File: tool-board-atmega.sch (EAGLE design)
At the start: 85 parts, among them IC3 ATMEGA2560-16AU, IC4 ATMEGA8U2-MU, Q1 16MHz, Q2 16MHz, X1 22-23-2031, X3 22-23-2031, X4 22-23-2031, X5 22-23-2021, X6 22-23-2021, X7 22-23-2021, X8 22-23-2021, X9 22-23-2101, Y1 16MHz, Y2 16MHz

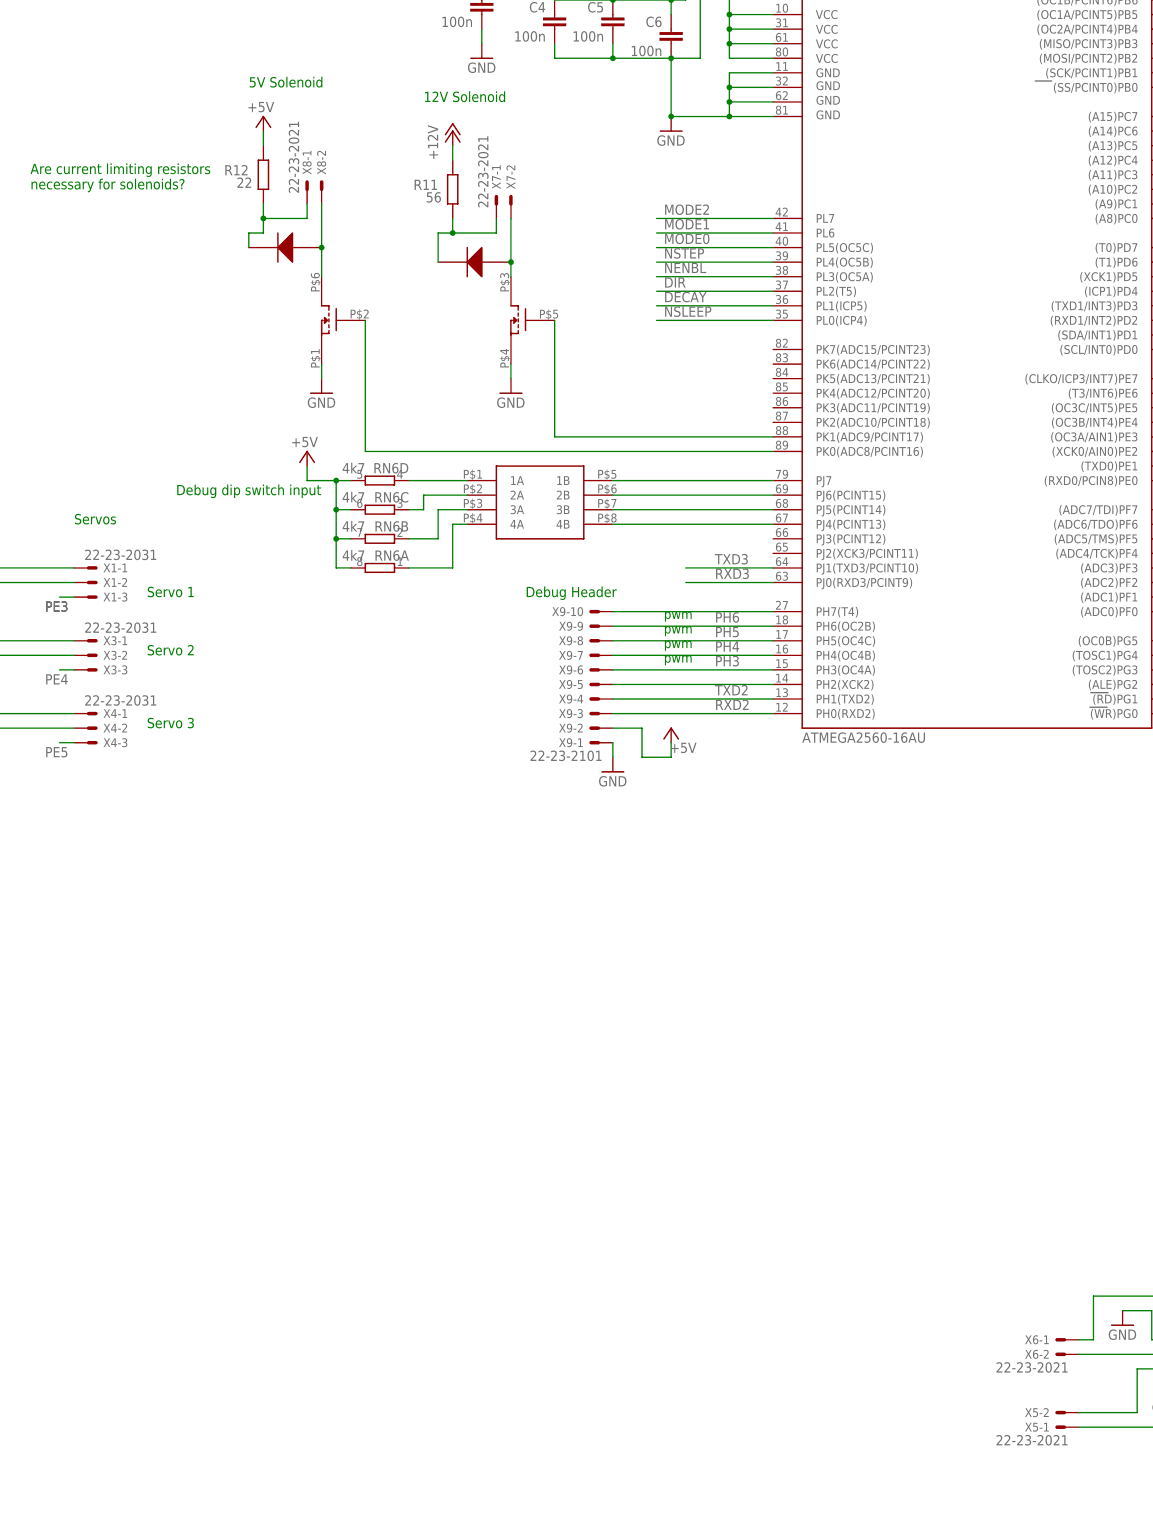
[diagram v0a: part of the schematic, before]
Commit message: board outline planned, some larger parts placed, schematic naming tweaks
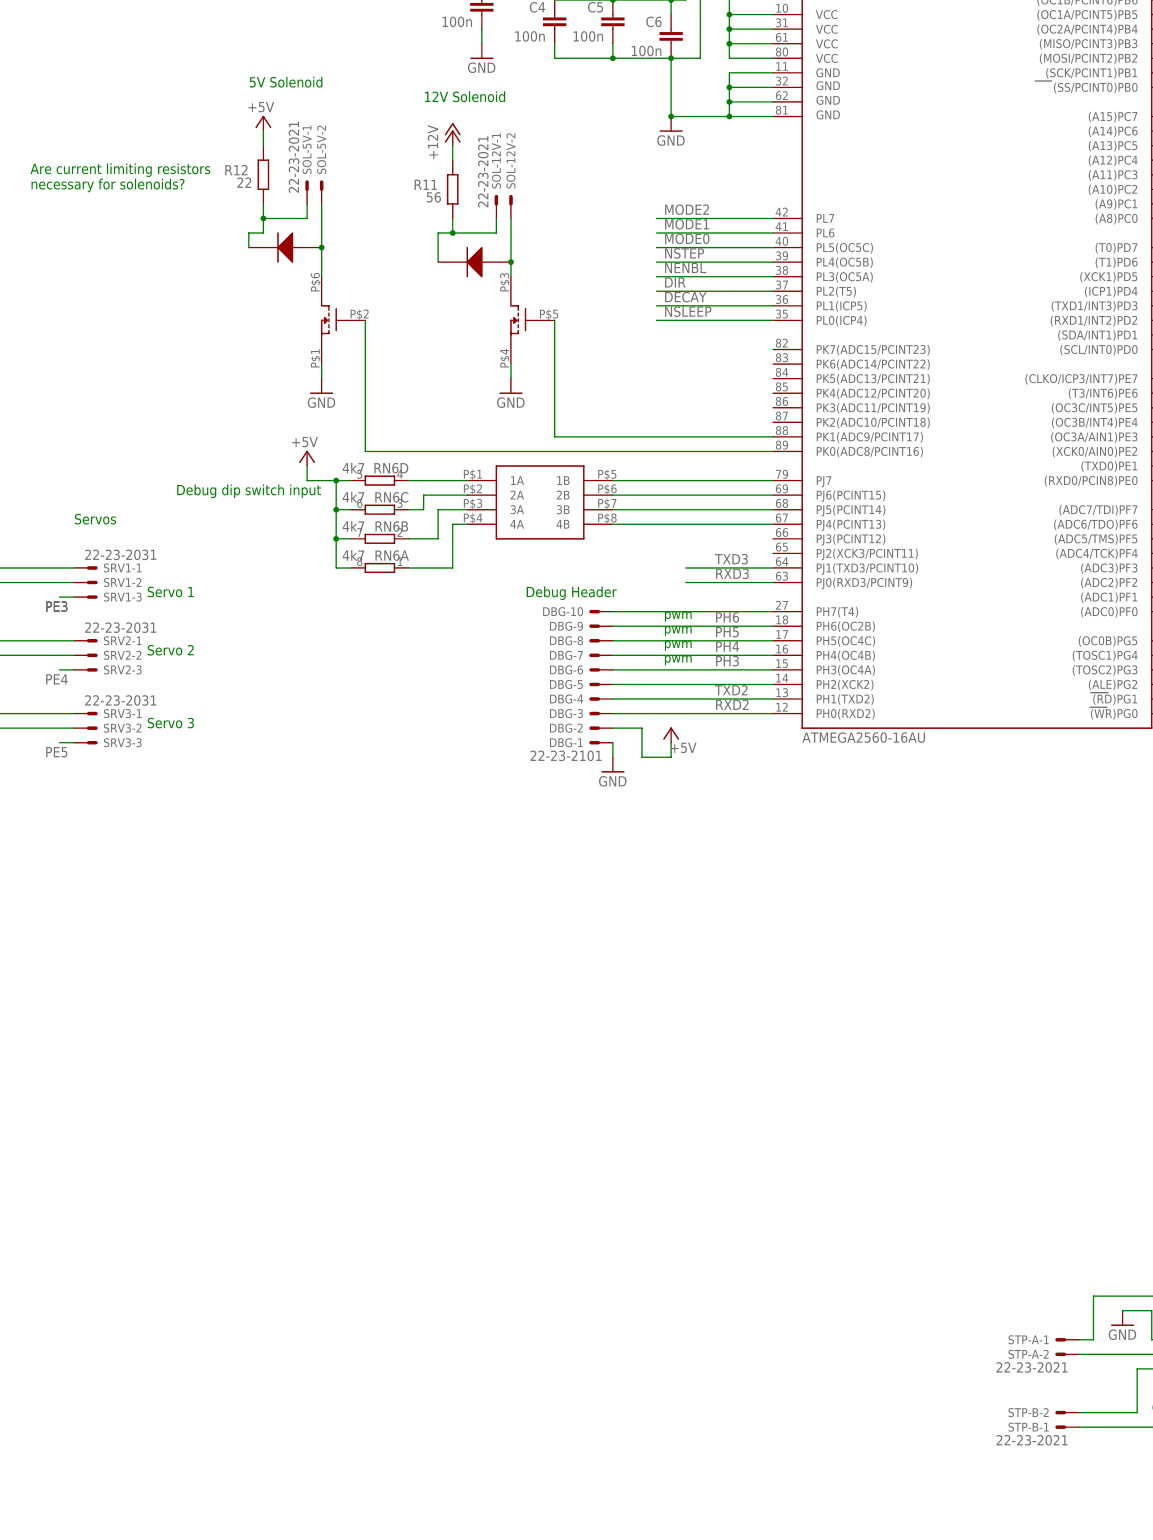
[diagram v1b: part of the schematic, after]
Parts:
- renumbered X1 to SRV1, X3 to SRV2, X4 to SRV3, X5 to STP-B, X6 to STP-A, X7 to SOL-12V, X8 to SOL-5V, X9 to DBG

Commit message: schematic revision edits - thanks Jaden
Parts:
- removed R5: 27R, SmartPrj:R-EU_R0603
- added R13, R15: 1M, SmartPrj:R-EU_R0603
- added R14, R16: 100, SmartPrj:R-EU_R0603
- RN6: value 4k7 -> 2k2
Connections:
- new net N$2: R14.1, U$15G$1.G
- new net N$36: R16.1, U$15G$2.G
- net +5V: no longer RN6A.2, RN6B.2, RN6C.2, RN6D.2
- net GND: now also R13.2, R15.2, RN6A.2, RN6B.2, RN6C.2, RN6D.2
- net N$15: now also R15.1, R16.2; no longer U$15G$2.G
- net N$16: now also R13.1, R14.2; no longer U$15G$1.G
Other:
- moved on the sheet: R11, R12, SOL-12V-1, SOL-12V-2, SOL-5V-1, SOL-5V-2

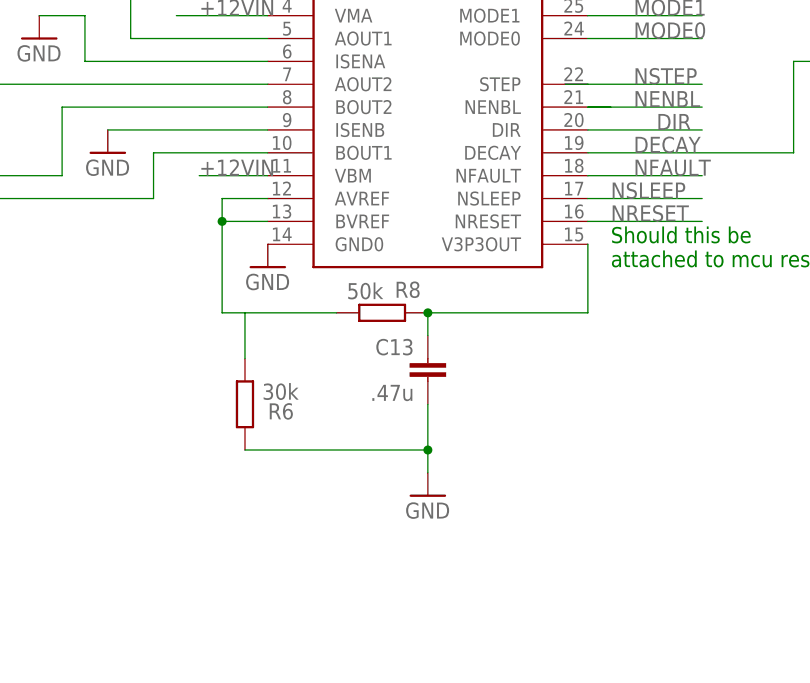
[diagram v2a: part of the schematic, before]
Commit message: library updates, changed diode package, added heat pad to DRV8825
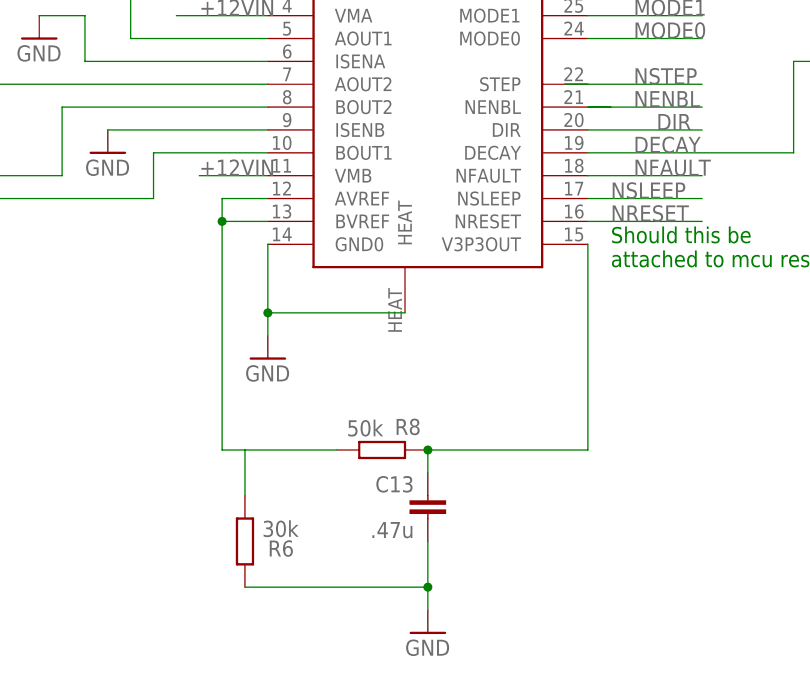
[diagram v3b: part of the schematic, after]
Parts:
- U$16, U$17: value DIODE_SOD323 -> DIODE0805; device ClinicalRobotics:DIODE_SOD323 -> ClinicalRobotics:DIODE0805
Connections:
- net +12VIN: now also U$1.VMB; no longer U$1.VBM
- net GND: now also U$1.HEAT
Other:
- moved on the sheet: C13, R6, R8
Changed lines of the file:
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@@
 <part name="R11" library="SmartPrj" deviceset="R-EU_" device="R0603" value="56"/>
 <part name="R12" library="SmartPrj" deviceset="R-EU_" device="R0603" value="22"/>
-<part name="U$16" library="ClinicalRobotics" deviceset="DIODE_SOD323" device=""/>
-<part name="U$17" library="ClinicalRobotics" deviceset="DIODE_SOD323" device=""/>
+<part name="U$16" library="ClinicalRobotics" deviceset="DIODE0805" device=""/>
+<part name="U$17" library="ClinicalRobotics" deviceset="DIODE0805" device=""/>
 <part name="DBG" library="con-molex" library_urn="urn:adsk.eagle:library:165" deviceset="22-23-2101" device="" package3d_urn="urn:adsk.eagle:package:8078641/1"/>
 <part name="GND19" library="supply1" deviceset="GND" device=""/>
@@
 <attribute name="VALUE" x="-38.1" y="-30.48" size="1.778" layer="96"/>
 </instance>
-<instance part="GND4" gate="1" x="190.5" y="-144.78" smashed="yes">
-<attribute name="VALUE" x="187.96" y="-147.32" size="1.778" layer="96"/>
+<instance part="GND4" gate="1" x="190.5" y="-154.94" smashed="yes">
+<attribute name="VALUE" x="187.96" y="-157.48" size="1.778" layer="96"/>
 </instance>
 <instance part="GND5" gate="1" x="233.68" y="-101.6" smashed="yes">
@@
 <attribute name="VALUE" x="194.945" y="-65.532" size="1.778" layer="96"/>
 </instance>
-<instance part="C13" gate="G$1" x="208.28" y="-154.94" smashed="yes" rot="MR0">
-<attribute name="NAME" x="206.756" y="-154.559" size="1.778" layer="95" rot="MR0"/>
-<attribute name="VALUE" x="206.756" y="-159.639" size="1.778" layer="96" rot="MR0"/>
-</instance>
-<instance part="GND6" gate="1" x="208.28" y="-170.18" smashed="yes">
-<attribute name="VALUE" x="205.74" y="-172.72" size="1.778" layer="96"/>
+<instance part="C13" gate="G$1" x="208.28" y="-170.18" smashed="yes" rot="MR0">
+<attribute name="NAME" x="206.756" y="-169.799" size="1.778" layer="95" rot="MR0"/>
+<attribute name="VALUE" x="206.756" y="-174.879" size="1.778" layer="96" rot="MR0"/>
+</instance>
+<instance part="GND6" gate="1" x="208.28" y="-185.42" smashed="yes">
+<attribute name="VALUE" x="205.74" y="-187.96" size="1.778" layer="96"/>
 </instance>
 <instance part="P+12" gate="1" x="205.74" y="-50.8" smashed="yes">
@@
 <attribute name="NAME" x="152.4" y="-123.698" size="1.524" layer="95" rot="R180"/>
 </instance>
-<instance part="R6" gate="G$1" x="187.96" y="-160.02" smashed="yes" rot="R270">
-<attribute name="NAME" x="190.5" y="-161.6964" size="1.778" layer="95"/>
-<attribute name="VALUE" x="189.865" y="-159.512" size="1.778" layer="96"/>
-</instance>
-<instance part="R8" gate="G$1" x="203.2" y="-149.86" smashed="yes">
-<attribute name="NAME" x="207.518" y="-146.4056" size="1.778" layer="95" rot="R180"/>
-<attribute name="VALUE" x="203.327" y="-146.558" size="1.778" layer="96" rot="R180"/>
+<instance part="R6" gate="G$1" x="187.96" y="-175.26" smashed="yes" rot="R270">
+<attribute name="NAME" x="190.5" y="-176.9364" size="1.778" layer="95"/>
+<attribute name="VALUE" x="189.865" y="-174.752" size="1.778" layer="96"/>
+</instance>
+<instance part="R8" gate="G$1" x="203.2" y="-165.1" smashed="yes">
+<attribute name="NAME" x="207.518" y="-161.6456" size="1.778" layer="95" rot="R180"/>
+<attribute name="VALUE" x="203.327" y="-161.798" size="1.778" layer="96" rot="R180"/>
 </instance>
 <instance part="GND9" gate="1" x="172.72" y="-132.08" smashed="yes">
@@
 <pinref part="GND4" gate="1" pin="GND"/>
 <pinref part="U$1" gate="G$1" pin="GND0"/>
+<wire x1="190.5" y1="-152.4" x2="190.5" y2="-149.86" width="0.1524" layer="91"/>
+<pinref part="U$1" gate="G$1" pin="HEAT"/>
+<wire x1="190.5" y1="-149.86" x2="190.5" y2="-142.24" width="0.1524" layer="91"/>
+<wire x1="205.74" y1="-149.86" x2="190.5" y2="-149.86" width="0.1524" layer="91"/>
+<junction x="190.5" y="-149.86"/>
 </segment>
 <segment>
@@
 <pinref part="GND6" gate="1" pin="GND"/>
 <pinref part="C13" gate="G$1" pin="2"/>
-<wire x1="208.28" y1="-167.64" x2="208.28" y2="-165.1" width="0.1524" layer="91"/>
+<wire x1="208.28" y1="-182.88" x2="208.28" y2="-180.34" width="0.1524" layer="91"/>
 <pinref part="R6" gate="G$1" pin="2"/>
-<wire x1="208.28" y1="-165.1" x2="208.28" y2="-160.02" width="0.1524" layer="91"/>
-<wire x1="187.96" y1="-165.1" x2="208.28" y2="-165.1" width="0.1524" layer="91"/>
-<junction x="208.28" y="-165.1"/>
+<wire x1="208.28" y1="-180.34" x2="208.28" y2="-175.26" width="0.1524" layer="91"/>
+<wire x1="187.96" y1="-180.34" x2="208.28" y2="-180.34" width="0.1524" layer="91"/>
+<junction x="208.28" y="-180.34"/>
 </segment>
 <segment>
@@
 <pinref part="C13" gate="G$1" pin="1"/>
 <pinref part="U$1" gate="G$1" pin="V3P3OUT"/>
-<wire x1="208.28" y1="-152.4" x2="208.28" y2="-149.86" width="0.1524" layer="91"/>
-<wire x1="208.28" y1="-149.86" x2="226.06" y2="-149.86" width="0.1524" layer="91"/>
-<wire x1="226.06" y1="-149.86" x2="226.06" y2="-142.24" width="0.1524" layer="91"/>
+<wire x1="208.28" y1="-167.64" x2="208.28" y2="-165.1" width="0.1524" layer="91"/>
+<wire x1="208.28" y1="-165.1" x2="226.06" y2="-165.1" width="0.1524" layer="91"/>
+<wire x1="226.06" y1="-165.1" x2="226.06" y2="-142.24" width="0.1524" layer="91"/>
 <pinref part="R8" gate="G$1" pin="2"/>
-<junction x="208.28" y="-149.86"/>
+<junction x="208.28" y="-165.1"/>
 </segment>
 </net>
@@
 </segment>
 <segment>
-<pinref part="U$1" gate="G$1" pin="VBM"/>
+<pinref part="U$1" gate="G$1" pin="VMB"/>
 <wire x1="190.5" y1="-134.62" x2="182.88" y2="-134.62" width="0.1524" layer="91"/>
 <label x="182.88" y="-134.62" size="1.778" layer="95"/>
@@
 <wire x1="185.42" y1="-137.16" x2="185.42" y2="-139.7" width="0.1524" layer="91"/>
 <junction x="185.42" y="-139.7"/>
-<wire x1="185.42" y1="-139.7" x2="185.42" y2="-149.86" width="0.1524" layer="91"/>
+<wire x1="185.42" y1="-139.7" x2="185.42" y2="-165.1" width="0.1524" layer="91"/>
 <pinref part="R8" gate="G$1" pin="1"/>
-<wire x1="198.12" y1="-149.86" x2="187.96" y2="-149.86" width="0.1524" layer="91"/>
+<wire x1="198.12" y1="-165.1" x2="187.96" y2="-165.1" width="0.1524" layer="91"/>
 <pinref part="R6" gate="G$1" pin="1"/>
-<wire x1="187.96" y1="-149.86" x2="187.96" y2="-154.94" width="0.1524" layer="91"/>
-<wire x1="185.42" y1="-149.86" x2="187.96" y2="-149.86" width="0.1524" layer="91"/>
-</segment>
-</net>
+<wire x1="187.96" y1="-165.1" x2="187.96" y2="-170.18" width="0.1524" layer="91"/>
+<wire x1="185.42" y1="-165.1" x2="187.96" y2="-165.1" width="0.1524" layer="91"/>
+</segment>
+</net>

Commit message: riped up and started layout over, organized components into logical systems
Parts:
- removed U$14: 4A, ClinicalRobotics:FUSE0805
- added C19, C22: 100uF, rcl:CPOL-USE3.5-8
- added F2: 500mA, rcl:L-EUL1812
- C18: device SmartPrj:C-EU0603-RND -> rcl:CPOL-USE3.5-8
- X2: value (none) -> MICROUSB_VERTICAL; device SmartPrj:PN61729 -> ClinicalRobotics:MICROUSB_VERTICAL
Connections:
- removed net XVCC: F1.2, U$9.P$1, X2.1
- new net VCCPIN: F1.2, F2.2, U$9.P$1, X2.1
- net +12V: now also C19.+; no longer U$14.P$2
- net +12VIN: now also C18.+; no longer C18.1, U$14.P$1
- net +5V: now also C22.+, F2.1
- net DECAY: now also IC3.PL6; no longer IC3.PL1(ICP5)
- net DIR: now also IC3.PL5(OC5C); no longer IC3.PL2(T5)
- net GND: now also C18.-, C19.-, C22.-; no longer C18.2
- net MODE0: now also IC3.PL2(T5); no longer IC3.PL5(OC5C)
- net MODE1: now also IC3.PL1(ICP5); no longer IC3.PL6
- net MODE2: now also IC3.PL0(ICP4); no longer IC3.PL7
- net NENBL: now also IC3.PL4(OC5B); no longer IC3.PL3(OC5A)
- net NSLEEP: now also IC3.PL7; no longer IC3.PL0(ICP4)
- net NSTEP: now also IC3.PL3(OC5A); no longer IC3.PL4(OC5B)
